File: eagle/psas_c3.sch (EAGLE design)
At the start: 77 parts, among them IC1 CP2102, U1 MIC5219 3.3V, Y1 32MHz

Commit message: First few changes submitted
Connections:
- removed net PTA20/!RESET: C21.1, JTAG1.10, R1.1, S2.1, U$1.PTA20/!RESET
- new net N$15: C21.1, R1.1, S2.1
- new net N$24: C1.1
- new net N$26: LED1.COMMON_ANODE, U2./TE, U2.SEL, U2.VIN1, U2.VIN2, U2.VPCC
- new net RESET: JTAG1.10, U$1.PTA20/!RESET
- net PTA1: no longer IC1.RXD
- net PTA18: no longer JP2.1
- net PTA2: no longer IC1.TXD
- net VBUS: no longer C1.1, LED1.COMMON_ANODE, U2./TE, U2.SEL, U2.VIN1, U2.VIN2, U2.VPCC
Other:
- moved on the sheet: ANT1, C1, C10, C11, C12, C13, C14, C15, C16, C17, C18, C19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

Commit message: Added a few more recommended things to the schematic
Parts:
- removed C9: 100nF, Vibrogait_prototype:C-EU0603-B-NOSILK
- removed Y1: 32MHz, Lilypad_Arduino_USB_v12:SPARKFUN-FREQCTRL_RESONATOR16MHZ
- added C22, C26: 11pF, Vibrogait_prototype:C-EU0603-B-NOSILK
- added C27, C28: 100nF, Vibrogait_prototype:C-EU0603-B-NOSILK
- added Q1: 32 MHz, crystal:FC-12M
- added R6: 0, rcl_custom:R-US_0603-B-NOSILK
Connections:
- removed net N$11: U$1.XTB, Y1.1
- net 3.3V: no longer C9.1, U$1.VREFH
- net GND: now also C26.2, C27.2, C28.2; no longer C9.2, Y1.2
- net N$12: now also Q1.2; no longer U$1.XTA, Y1.3
- net PTD5: no longer IC1.CTS
- net PTD6: no longer IC1.RTS
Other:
- note added: "32 MHz Crystal"
- note added: "Bidirectional Transceiver Circuit at 436.5MHz"
- note added: "NC"
- note removed: "Bidirectional Transceiver Circuit at 435MHz"
- moved on the sheet: C8

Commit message: Fixed alignment issues on schematic
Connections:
- removed net N$24: C1.1
- removed net N$26: LED1.COMMON_ANODE, U2./TE, U2.SEL, U2.VIN1, U2.VIN2, U2.VPCC
- new net N$11: R6.2, U$1.XTA
- net GND: now also C22.2
- net N$12: now also C22.1, R6.1
- net N$15: now also C26.1, Q1.1, U$1.XTB; no longer C21.1, R1.1, S2.1
- net RESET: now also C21.1, R1.1, S2.1
- net VBUS: now also C1.1, LED1.COMMON_ANODE, U2./TE, U2.SEL, U2.VIN1, U2.VIN2, U2.VPCC
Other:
- moved on the sheet: C1, C21, C22, C26, C5, C6, Q1, R1, R6, S2, TP3, TP4

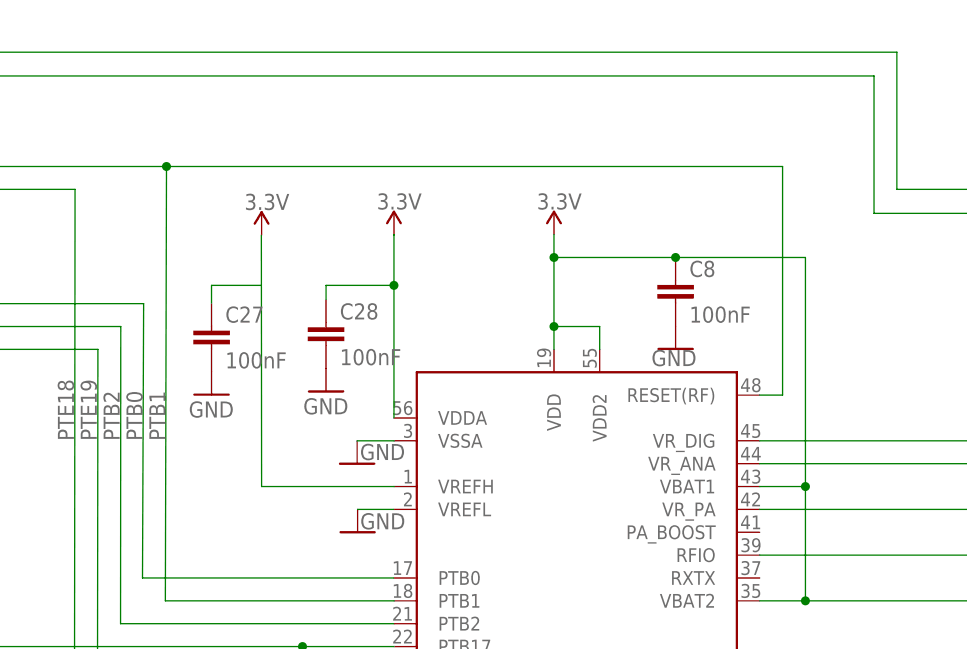
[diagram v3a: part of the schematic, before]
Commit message: Fixed alignment issues on schematic
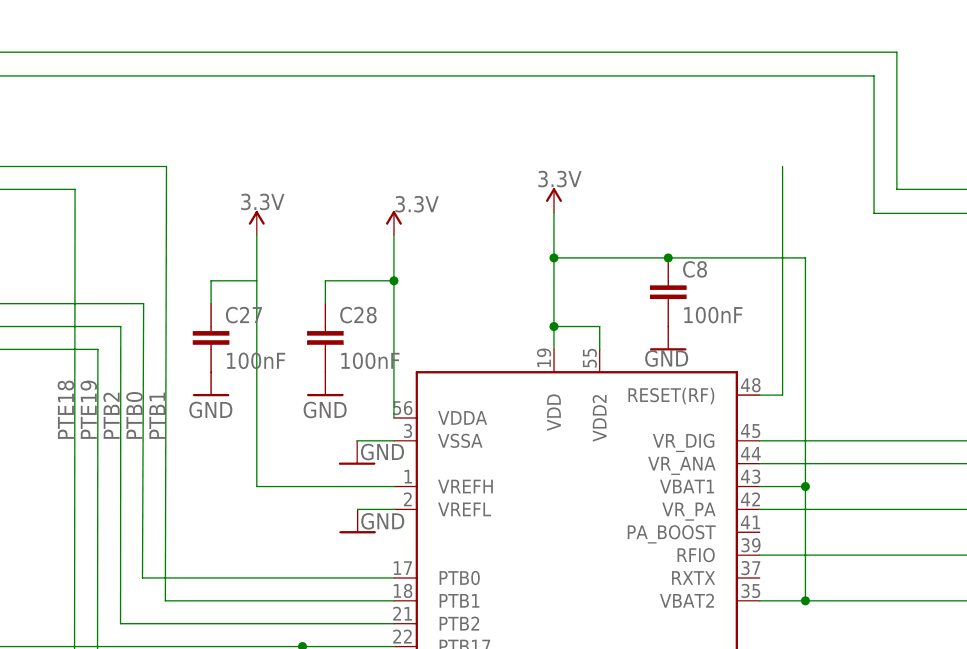
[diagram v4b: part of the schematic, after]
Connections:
- new net N$23: U$1.RESET(RF)
- net PTB1: no longer U$1.RESET(RF)
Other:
- moved on the sheet: C8
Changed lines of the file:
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@@
 </instance>
 <instance part="GND14" gate="1" x="235.6612" y="223.4946"/>
-<instance part="P+2" gate="G$1" x="203.2" y="279.4508" smashed="yes">
-<attribute name="VALUE" x="201.295" y="282.2448" size="1.778" layer="96"/>
-</instance>
-<instance part="C8" gate="CE" x="216.7128" y="274.3708">
-<attribute name="DIST" x="216.7128" y="274.3708" size="1.778" layer="96" display="off"/>
-<attribute name="DPN" x="216.7128" y="274.3708" size="1.778" layer="96" display="off"/>
-<attribute name="MFG" x="216.7128" y="274.3708" size="1.778" layer="96" display="off"/>
-<attribute name="MPN" x="216.7128" y="274.3708" size="1.778" layer="96" display="off"/>
+<instance part="P+2" gate="G$1" x="203.2" y="281.94" smashed="yes">
+<attribute name="VALUE" x="201.295" y="284.734" size="1.778" layer="96"/>
+</instance>
+<instance part="C8" gate="CE" x="215.9" y="274.32">
+<attribute name="DIST" x="215.9" y="274.32" size="1.778" layer="96" display="off"/>
+<attribute name="DPN" x="215.9" y="274.32" size="1.778" layer="96" display="off"/>
+<attribute name="MFG" x="215.9" y="274.32" size="1.778" layer="96" display="off"/>
+<attribute name="MPN" x="215.9" y="274.32" size="1.778" layer="96" display="off"/>
 </instance>
 <instance part="CF1" gate="CF" x="35.56" y="342.9" rot="MR270"/>
@@
 <attribute name="VALUE" x="181.6608" y="246.7102" size="1.778" layer="96"/>
 </instance>
-<instance part="P+6" gate="G$1" x="170.7134" y="279.4" smashed="yes">
-<attribute name="VALUE" x="168.8084" y="282.194" size="1.778" layer="96"/>
-</instance>
-<instance part="C27" gate="CE" x="165.1508" y="269.2908">
-<attribute name="DIST" x="165.1508" y="269.2908" size="1.778" layer="96" display="off"/>
-<attribute name="DPN" x="165.1508" y="269.2908" size="1.778" layer="96" display="off"/>
-<attribute name="MFG" x="165.1508" y="269.2908" size="1.778" layer="96" display="off"/>
-<attribute name="MPN" x="165.1508" y="269.2908" size="1.778" layer="96" display="off"/>
-</instance>
-<instance part="GND30" gate="1" x="165.1508" y="261.6708"/>
-<instance part="P+7" gate="G$1" x="185.42" y="279.4508" smashed="yes">
-<attribute name="VALUE" x="183.515" y="282.2448" size="1.778" layer="96"/>
-</instance>
-<instance part="C28" gate="CE" x="177.8762" y="269.6464">
-<attribute name="DIST" x="177.8762" y="269.6464" size="1.778" layer="96" display="off"/>
-<attribute name="DPN" x="177.8762" y="269.6464" size="1.778" layer="96" display="off"/>
-<attribute name="MFG" x="177.8762" y="269.6464" size="1.778" layer="96" display="off"/>
-<attribute name="MPN" x="177.8762" y="269.6464" size="1.778" layer="96" display="off"/>
-</instance>
-<instance part="GND35" gate="1" x="177.8762" y="262.0264"/>
-<instance part="GND12" gate="1" x="216.7128" y="266.7508" smashed="yes">
-<attribute name="VALUE" x="214.0204" y="264.8458" size="1.778" layer="96"/>
+<instance part="P+6" gate="G$1" x="170.18" y="279.4" smashed="yes">
+<attribute name="VALUE" x="168.275" y="282.194" size="1.778" layer="96"/>
+</instance>
+<instance part="C27" gate="CE" x="165.1" y="269.24">
+<attribute name="DIST" x="165.1" y="269.24" size="1.778" layer="96" display="off"/>
+<attribute name="DPN" x="165.1" y="269.24" size="1.778" layer="96" display="off"/>
+<attribute name="MFG" x="165.1" y="269.24" size="1.778" layer="96" display="off"/>
+<attribute name="MPN" x="165.1" y="269.24" size="1.778" layer="96" display="off"/>
+</instance>
+<instance part="GND30" gate="1" x="165.1" y="261.62"/>
+<instance part="P+7" gate="G$1" x="185.42" y="279.4" smashed="yes">
+<attribute name="VALUE" x="185.42" y="281.94" size="1.778" layer="96"/>
+</instance>
+<instance part="C28" gate="CE" x="177.8" y="269.24">
+<attribute name="DIST" x="177.8" y="269.24" size="1.778" layer="96" display="off"/>
+<attribute name="DPN" x="177.8" y="269.24" size="1.778" layer="96" display="off"/>
+<attribute name="MFG" x="177.8" y="269.24" size="1.778" layer="96" display="off"/>
+<attribute name="MPN" x="177.8" y="269.24" size="1.778" layer="96" display="off"/>
+</instance>
+<instance part="GND35" gate="1" x="177.8" y="261.62"/>
+<instance part="GND12" gate="1" x="215.9" y="266.7" smashed="yes">
+<attribute name="VALUE" x="213.2076" y="264.795" size="1.778" layer="96"/>
 </instance>
 </instances>
@@
 </segment>
 <segment>
-<wire x1="185.42" y1="279.4508" x2="185.42" y2="279.4" width="0.1524" layer="91"/>
 <pinref part="P+7" gate="G$1" pin="3.3V"/>
 <pinref part="U$1" gate="G$1" pin="VDDA"/>
-<wire x1="185.42" y1="259.08" x2="185.42" y2="273.812" width="0.1524" layer="91"/>
-<wire x1="185.42" y1="273.812" x2="185.42" y2="279.4508" width="0.1524" layer="91"/>
-<wire x1="177.8762" y1="272.2372" x2="177.8762" y2="273.812" width="0.1524" layer="91"/>
-<wire x1="177.8762" y1="273.812" x2="185.42" y2="273.812" width="0.1524" layer="91"/>
-<junction x="185.42" y="273.812"/>
+<wire x1="185.42" y1="259.08" x2="185.42" y2="274.32" width="0.1524" layer="91"/>
+<wire x1="185.42" y1="274.32" x2="185.42" y2="279.4" width="0.1524" layer="91"/>
+<wire x1="177.8" y1="271.78" x2="177.8" y2="274.32" width="0.1524" layer="91"/>
+<wire x1="177.8" y1="274.32" x2="185.42" y2="274.32" width="0.1524" layer="91"/>
+<junction x="185.42" y="274.32"/>
 </segment>
 <segment>
 <pinref part="U$1" gate="G$1" pin="VDD"/>
 <pinref part="P+2" gate="G$1" pin="3.3V"/>
-<wire x1="203.2" y1="279.4508" x2="203.2" y2="276.9108" width="0.1524" layer="91"/>
+<wire x1="203.2" y1="281.94" x2="203.2" y2="276.86" width="0.1524" layer="91"/>
 <pinref part="U$1" gate="G$1" pin="VDD2"/>
-<wire x1="203.2" y1="276.9108" x2="203.2" y2="269.24" width="0.1524" layer="91"/>
+<wire x1="203.2" y1="276.86" x2="203.2" y2="269.24" width="0.1524" layer="91"/>
 <wire x1="203.2" y1="269.24" x2="203.2" y2="266.7" width="0.1524" layer="91"/>
 <wire x1="203.2" y1="269.24" x2="208.28" y2="269.24" width="0.1524" layer="91"/>
 <wire x1="208.28" y1="269.24" x2="208.28" y2="266.7" width="0.1524" layer="91"/>
 <junction x="203.2" y="269.24"/>
-<junction x="203.2" y="276.9108"/>
-<wire x1="216.7128" y1="276.9108" x2="203.2" y2="276.9108" width="0.1524" layer="91"/>
+<junction x="203.2" y="276.86"/>
+<wire x1="215.9" y1="276.86" x2="203.2" y2="276.86" width="0.1524" layer="91"/>
 <pinref part="C8" gate="CE" pin="1"/>
 <pinref part="U$1" gate="G$1" pin="VBAT1"/>
 <wire x1="226.06" y1="251.46" x2="231.14" y2="251.46" width="0.1524" layer="91"/>
-<wire x1="231.14" y1="251.46" x2="231.14" y2="276.9108" width="0.1524" layer="91"/>
-<wire x1="231.14" y1="276.9108" x2="216.7128" y2="276.9108" width="0.1524" layer="91"/>
-<junction x="216.7128" y="276.9108"/>
+<wire x1="231.14" y1="251.46" x2="231.14" y2="276.86" width="0.1524" layer="91"/>
+<wire x1="231.14" y1="276.86" x2="215.9" y2="276.86" width="0.1524" layer="91"/>
+<junction x="215.9" y="276.86"/>
 <pinref part="U$1" gate="G$1" pin="VBAT2"/>
 <wire x1="226.06" y1="238.76" x2="231.14" y2="238.76" width="0.1524" layer="91"/>
@@
 <wire x1="160.147" y1="287.02" x2="43.434" y2="287.02" width="0.1524" layer="91"/>
 <label x="160.02" y="256.54" size="1.778" layer="95" rot="R90"/>
-<wire x1="160.147" y1="287.02" x2="228.6" y2="287.02" width="0.1524" layer="91"/>
-<wire x1="228.6" y1="287.02" x2="228.6" y2="261.62" width="0.1524" layer="91"/>
-<junction x="160.147" y="287.02"/>
-<pinref part="U$1" gate="G$1" pin="RESET(RF)"/>
-<wire x1="228.6" y1="261.62" x2="226.06" y2="261.62" width="0.1524" layer="91"/>
 </segment>
 </net>
@@
 <net name="VREFH" class="0">
 <segment>
-<wire x1="185.4454" y1="251.46" x2="170.7134" y2="251.46" width="0.1524" layer="91"/>
-<wire x1="170.7134" y1="251.46" x2="170.688" y2="279.4" width="0.1524" layer="91"/>
-</segment>
-<segment>
-<wire x1="165.1508" y1="271.8562" x2="165.1508" y2="273.812" width="0.1524" layer="91"/>
-<wire x1="165.1508" y1="273.812" x2="170.688" y2="273.812" width="0.1524" layer="91"/>
+<wire x1="185.4454" y1="251.46" x2="170.18" y2="251.46" width="0.1524" layer="91"/>
+<wire x1="170.18" y1="251.46" x2="170.18" y2="279.4" width="0.1524" layer="91"/>
+</segment>
+<segment>
+<wire x1="165.1" y1="271.78" x2="165.1" y2="274.32" width="0.1524" layer="91"/>
+<wire x1="165.1" y1="274.32" x2="170.18" y2="274.32" width="0.1524" layer="91"/>
 </segment>
 </net>
@@
 </segment>
 </net>
+<net name="N$23" class="0">
+<segment>
+<pinref part="U$1" gate="G$1" pin="RESET(RF)"/>
+<wire x1="228.6" y1="261.62" x2="226.06" y2="261.62" width="0.1524" layer="91"/>
+<wire x1="228.6" y1="287.02" x2="228.6" y2="261.62" width="0.1524" layer="91"/>
+</segment>
+</net>
